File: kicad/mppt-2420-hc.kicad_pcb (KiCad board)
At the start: 4 copper layers, 100 x 100 mm, 141 parts, among them J1 MKDS 5/ 2-9,5, J2 MKDS 5/ 2-9,5, J4 8P8C, J5 8P8C, J7 UEXT, P1 CONN_01X02, Q1 IPA045N10N3G, Q2 IPA045N10N3G, Q3 IPA045N10N3G, T1 BC846B, T10 BC846B, T3 BC846B, T4 BC856B, U1 LM5107, U2 STM32G431CBTx, U3 MPQ8112, U4 LMR16006X, U6 W25Q80DVS, U7 TCAN334, Y1 8MHz

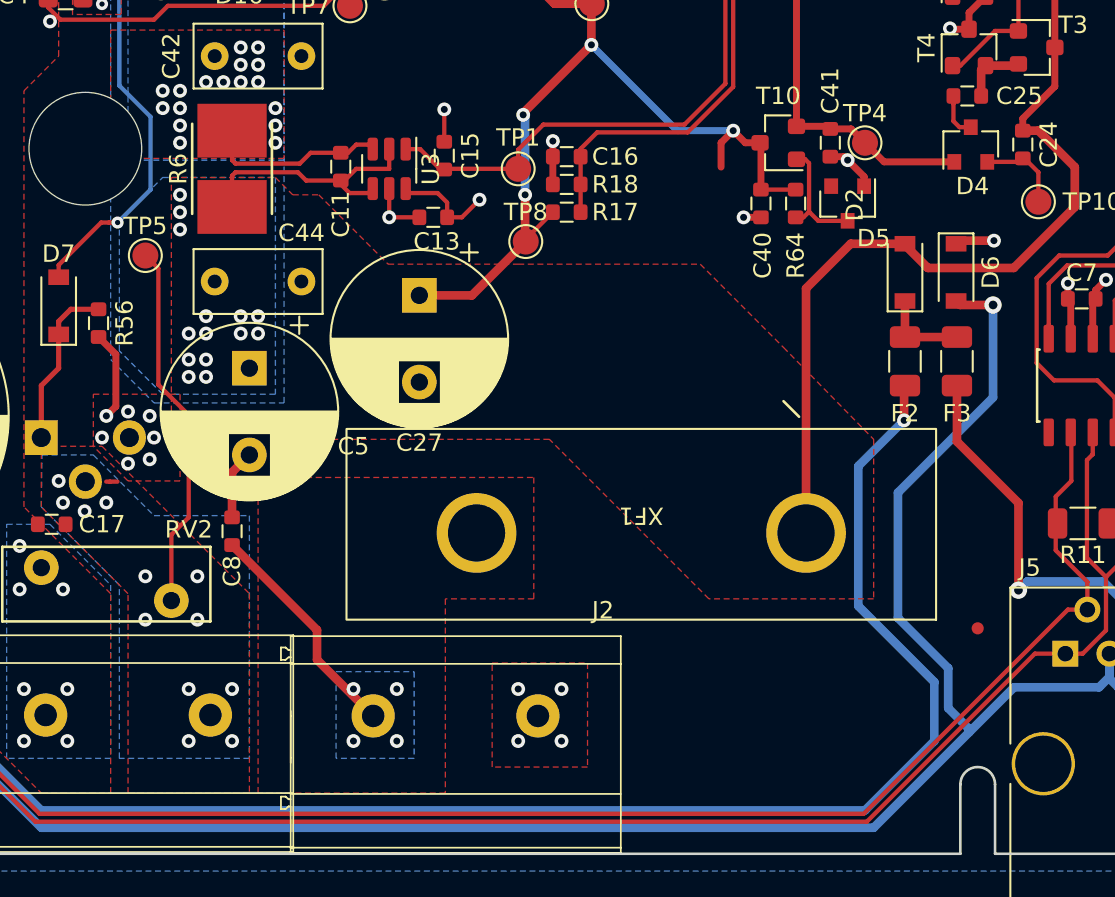
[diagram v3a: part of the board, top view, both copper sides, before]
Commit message: minor component name fix
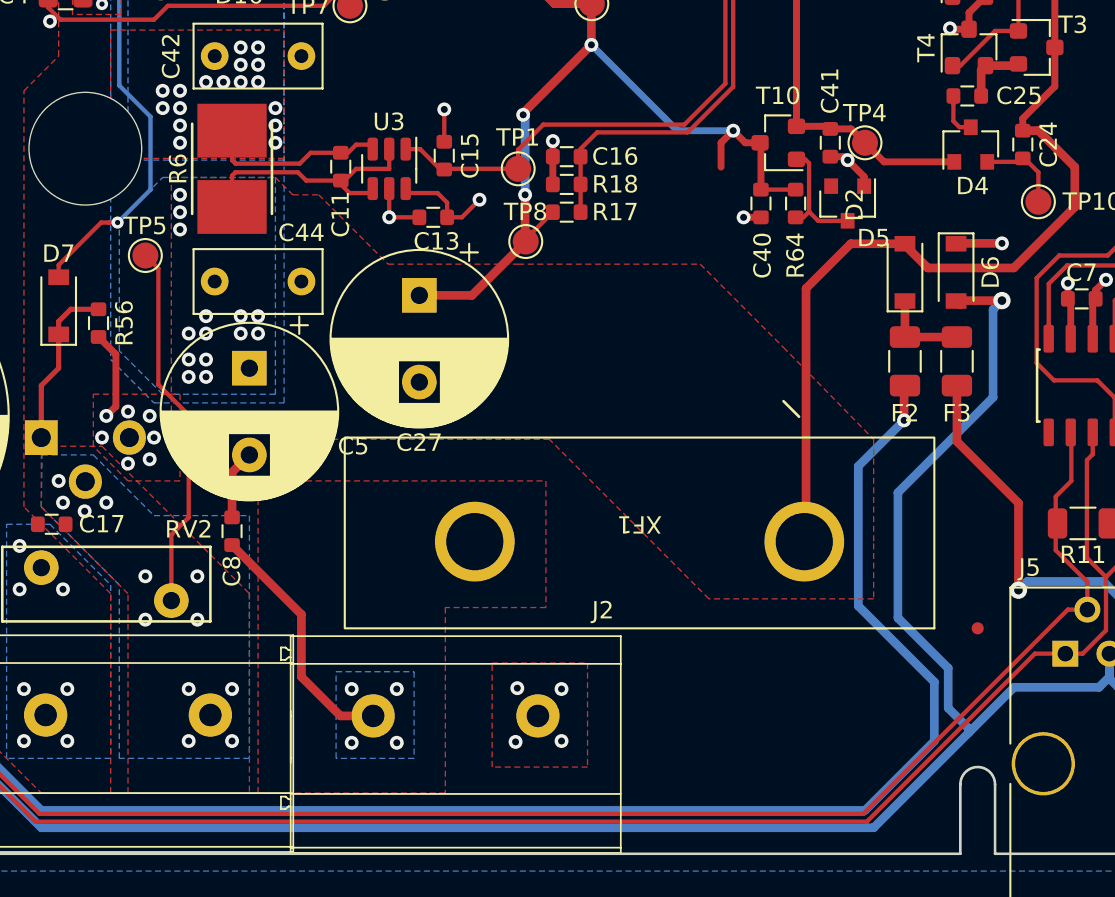
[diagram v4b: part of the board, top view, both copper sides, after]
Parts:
- XF1: footprint LibreSolar:Eaton_S-400 -> LibreSolar:Eaton_S-4000
- moved XF1 0.51 mm to (160.5, 122.0)
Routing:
- net /CAN_GND: track 128.3 -> 129.5 mm
- net /BAT+: track 13.2 -> 14.3 mm
- net /DCDC_HV-: track 22.0 -> 21.3 mm
- net GND: track 73.7 -> 74.4 mm
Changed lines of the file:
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@@
     )
   )
-  (footprint "LibreSolar:Eaton_S-400" (layer "F.Cu")
-    (at 160.6 121.5 180)
+  (footprint "LibreSolar:Eaton_S-4000" (layer "F.Cu")
+    (at 160.5 122 180)
     (property "Manufacturer" "Eaton")
     (property "PartNumber" "")
@@
     (property "Sheetname" "DC/DC")
     (attr smd)
-    (fp_text reference "U3" (at 0 -2.4 90) (layer "F.SilkS")
+    (fp_text reference "U3" (at -2.703 0.013) (layer "F.SilkS")
       (effects (font (size 1 1) (thickness 0.15)))
     )
@@
   (segment (start 185 79.3) (end 185 80.3) (width 0.4) (layer "F.Cu") (net 1))
   (segment (start 178.45 92.45) (end 178.4 92.4) (width 0.4) (layer "F.Cu") (net 1))
-  (segment (start 180.9372 104.6432) (end 178.9316 104.6432) (width 0.5) (layer "F.Cu") (net 1))
   (segment (start 175.1 71.4) (end 175.1 71.85) (width 0.25) (layer "F.Cu") (net 1))
   (segment (start 182.3 60.5) (end 183.300004 60.5) (width 0.25) (layer "F.Cu") (net 1))
@@
   (segment (start 171.5 99.8) (end 172.3 99.8) (width 0.4) (layer "F.Cu") (net 1))
   (segment (start 129.75 114.75) (end 130.3 114.2) (width 0.4) (layer "F.Cu") (net 1))
+  (segment (start 178.7748 104.8) (end 178.7528 104.822) (width 0.5) (layer "F.Cu") (net 1))
   (segment (start 179.5 92.45) (end 178.45 92.45) (width 0.4) (layer "F.Cu") (net 1))
   (segment (start 175.1 72.45) (end 174.85 72.2) (width 0.25) (layer "F.Cu") (net 1))
@@
   (segment (start 190.905 84.895) (end 190.9 84.9) (width 0.4) (layer "F.Cu") (net 1))
   (segment (start 168.2 62.3) (end 166.5 62.3) (width 0.4) (layer "F.Cu") (net 1))
+  (segment (start 181.4 104.8) (end 178.7748 104.8) (width 0.5) (layer "F.Cu") (net 1))
   (segment (start 175.1 71.4) (end 175.1 69.9) (width 0.25) (layer "F.Cu") (net 1))
   (segment (start 186.8 108) (end 186.8 107.499996) (width 0.4) (layer "F.Cu") (net 1))
@@
   (via (at 182 76.8) (size 0.8) (drill 0.4) (layers "F.Cu" "B.Cu") (net 1))
   (via (at 186.3 75.5) (size 0.8) (drill 0.4) (layers "F.Cu" "B.Cu") (net 1))
-  (via (at 180.9372 104.6432) (size 0.8) (drill 0.4) (layers "F.Cu" "B.Cu") (net 1))
+  (via (at 181.4 104.8) (size 0.8) (drill 0.4) (layers "F.Cu" "B.Cu") (net 1))
   (via (at 116.5 117) (size 0.8) (drill 0.4) (layers "F.Cu" "B.Cu") (net 1))
   (via (at 124.8 81.2) (size 0.8) (drill 0.4) (layers "F.Cu" "B.Cu") (net 1))
   (via (at 129.5 91) (size 0.7) (drill 0.3) (layers "F.Cu" "B.Cu") (net 1))
   (via (at 187.8 61.7) (size 0.8) (drill 0.4) (layers "F.Cu" "B.Cu") (net 1))
-  (via (at 153.5 130.5) (size 0.8) (drill 0.4) (layers "F.Cu" "B.Cu") (net 1))
+  (via (at 153.45 130.45) (size 0.8) (drill 0.4) (layers "F.Cu" "B.Cu") (net 1))
   (via (at 132.25 117.25) (size 0.8) (drill 0.4) (layers "F.Cu" "B.Cu") (net 1))
   (via (at 172.5 57.7) (size 0.8) (drill 0.4) (layers "F.Cu" "B.Cu") (net 1))
@@
   (via (at 161.6 87.7) (size 0.8) (drill 0.4) (layers "F.Cu" "B.Cu") (net 1))
   (via (at 149.238 97.074) (size 0.8) (drill 0.4) (layers "F.Cu" "B.Cu") (net 1))
-  (via (at 153.5 133.5) (size 0.8) (drill 0.4) (layers "F.Cu" "B.Cu") (net 1))
+  (via (at 153.35 133.55) (size 0.8) (drill 0.4) (layers "F.Cu" "B.Cu") (net 1))
   (via (at 183.300004 60.5) (size 0.8) (drill 0.4) (layers "F.Cu" "B.Cu") (net 1))
   (via (at 108 97.5) (size 0.8) (drill 0.4) (layers "F.Cu" "B.Cu") (net 1))
@@
   (segment (start 164.850011 87.750011) (end 165.449989 88.349989) (width 0.25) (layer "F.Cu") (net 30))
   (segment (start 170.897887 63.75) (end 168.3 66.347887) (width 0.25) (layer "F.Cu") (net 30))
-  (segment (start 141.9 127.1) (end 141.9 128.811) (width 0.5) (layer "F.Cu") (net 31))
-  (segment (start 141.9 128.811) (end 145.139 132.05) (width 0.5) (layer "F.Cu") (net 31))
-  (segment (start 137 122.2) (end 141.9 127.1) (width 0.5) (layer "F.Cu") (net 31))
-  (via (at 146.5 133.5) (size 0.8) (drill 0.4) (layers "F.Cu" "B.Cu") (net 31))
-  (via (at 144 130.5) (size 0.8) (drill 0.4) (layers "F.Cu" "B.Cu") (net 31))
+  (segment (start 145.139 132.05) (end 143.25 132.05) (width 0.5) (layer "F.Cu") (net 31))
+  (segment (start 141 129.8) (end 141 126.2) (width 0.5) (layer "F.Cu") (net 31))
+  (segment (start 143.25 132.05) (end 141 129.8) (width 0.5) (layer "F.Cu") (net 31))
+  (segment (start 141 126.2) (end 137 122.2) (width 0.5) (layer "F.Cu") (net 31))
+  (via (at 146.5 133.6) (size 0.8) (drill 0.4) (layers "F.Cu" "B.Cu") (net 31))
+  (via (at 143.9 130.5) (size 0.8) (drill 0.4) (layers "F.Cu" "B.Cu") (net 31))
   (via (at 146.5 130.5) (size 0.8) (drill 0.4) (layers "F.Cu" "B.Cu") (net 31))
-  (via (at 144 133.5) (size 0.8) (drill 0.4) (layers "F.Cu" "B.Cu") (net 31))
+  (via (at 143.9 133.6) (size 0.8) (drill 0.4) (layers "F.Cu" "B.Cu") (net 31))
   (segment (start 127 112) (end 127 110.05) (width 0.3) (layer "F.Cu") (net 32))
   (segment (start 126 116) (end 126 113) (width 0.3) (layer "F.Cu") (net 32))
@@
   (segment (start 162.670144 98.3) (end 157.722412 93.352268) (width 0.4) (layer "B.Cu") (net 37))
   (segment (start 152.799994 81.465685) (end 152.799994 80.9) (width 0.5) (layer "B.Cu") (net 37))
-  (segment (start 129.96 118.54) (end 129.7425 118.54) (width 0.25) (layer "F.Cu") (net 38))
-  (segment (start 130.394171 118.54) (end 129.96 118.54) (width 0.25) (layer "F.Cu") (net 38))
   (segment (start 134.5 120.6) (end 133.5 121.6) (width 0.25) (layer "F.Cu") (net 38))
   (segment (start 132.749999 112.949999) (end 134.5 114.7) (width 0.25) (layer "F.Cu") (net 38))
@@
   (via (at 137.5 95.5) (size 0.8) (drill 0.4) (layers "F.Cu" "B.Cu") (net 47))
   (via (at 136.5 74.5) (size 0.8) (drill 0.4) (layers "F.Cu" "B.Cu") (net 47))
-  (segment (start 180.8864 108.3516) (end 178.9824 108.3516) (width 0.5) (layer "F.Cu") (net 48))
+  (segment (start 178.7748 108.1) (end 178.7528 108.122) (width 0.5) (layer "F.Cu") (net 48))
   (segment (start 178.9824 108.3516) (end 178.7528 108.122) (width 0.5) (layer "F.Cu") (net 48))
-  (via (at 180.8864 108.3516) (size 1) (drill 0.5) (layers "F.Cu" "B.Cu") (net 48))
+  (segment (start 181.4 108.1) (end 178.7748 108.1) (width 0.5) (layer "F.Cu") (net 48))
+  (via (at 181.4 108.1) (size 1) (drill 0.5) (layers "F.Cu" "B.Cu") (net 48))
   (segment (start 112.925001 129.209999) (end 113.675 128.46) (width 0.5) (layer "B.Cu") (net 48))
   (segment (start 187 130.4) (end 187.595 129.805) (width 0.5) (layer "B.Cu") (net 48))
   (segment (start 187.595 129.805) (end 187.595 128.46) (width 0.5) (layer "B.Cu") (net 48))
-  (segment (start 178.3 129.3) (end 178.3 131.6) (width 0.5) (layer "B.Cu") (net 48))
-  (segment (start 180.8864 113.6856) (end 175.4 119.172) (width 0.5) (layer "B.Cu") (net 48))
+  (segment (start 179.5 132.8) (end 179.5 133) (width 0.5) (layer "B.Cu") (net 48))
+  (segment (start 180.8864 108.6136) (end 180.8864 113.6856) (width 0.5) (layer "B.Cu") (net 48))
   (segment (start 188.1 130.4) (end 192.1 130.4) (width 0.5) (layer "B.Cu") (net 48))
   (segment (start 108.595 128.46) (end 109.795001 129.660001) (width 0.5) (layer "B.Cu") (net 48))
-  (segment (start 179.5 132.8) (end 179.5 133) (width 0.5) (layer "B.Cu") (net 48))
+  (segment (start 178.3 129.3) (end 178.3 131.6) (width 0.5) (layer "B.Cu") (net 48))
+  (segment (start 175.4 126.4) (end 178.3 129.3) (width 0.5) (layer "B.Cu") (net 48))
   (segment (start 174 138.5) (end 179.5 133) (width 0.5) (layer "B.Cu") (net 48))
+  (segment (start 180.8864 113.6856) (end 175.4 119.172) (width 0.5) (layer "B.Cu") (net 48))
   (segment (start 113.675 128.46) (end 115.965017 128.46) (width 0.5) (layer "B.Cu") (net 48))
   (segment (start 109.795001 129.660001) (end 112.474999 129.660001) (width 0.5) (layer "B.Cu") (net 48))
@@
   (segment (start 178.3 131.6) (end 179.5 132.8) (width 0.5) (layer "B.Cu") (net 48))
   (segment (start 126.005017 138.5) (end 174 138.5) (width 0.5) (layer "B.Cu") (net 48))
-  (segment (start 175.4 119.172) (end 175.4 126.4) (width 0.5) (layer "B.Cu") (net 48))
   (segment (start 192.1 130.4) (end 192.675 129.825) (width 0.5) (layer "B.Cu") (net 48))
-  (segment (start 180.8864 108.3516) (end 180.8864 113.6856) (width 0.5) (layer "B.Cu") (net 48))
+  (segment (start 175.4 119.172) (end 175.4 126.4) (width 0.5) (layer "B.Cu") (net 48))
   (segment (start 192.675 129.825) (end 192.675 128.46) (width 0.5) (layer "B.Cu") (net 48))
   (segment (start 112.474999 129.660001) (end 112.925001 129.209999) (width 0.5) (layer "B.Cu") (net 48))
-  (segment (start 175.4 126.4) (end 178.3 129.3) (width 0.5) (layer "B.Cu") (net 48))
   (segment (start 115.965017 128.46) (end 126.005017 138.5) (width 0.5) (layer "B.Cu") (net 48))
   (segment (start 187.595 128.46) (end 187.595 129.895) (width 0.5) (layer "B.Cu") (net 48))
+  (segment (start 181.4 108.1) (end 180.8864 108.6136) (width 0.5) (layer "B.Cu") (net 48))
   (segment (start 185.4 118.5) (end 184.5 119.4) (width 0.25) (layer "F.Cu") (net 49))
   (segment (start 173.42109 137.7) (end 185.20109 125.92) (width 0.25) (layer "F.Cu") (net 49))
@@
     (polygon
       (pts
-        (xy 154.4 125.3)
-        (xy 149.3 125.3)
+        (xy 155.1 125.8)
+        (xy 149.3 125.8)
         (xy 149.3 136.5)
         (xy 138.5 136.5)
-        (xy 138.5 118.3)
-        (xy 154.4 118.3)
+        (xy 138.5 118.5)
+        (xy 155.1 118.5)
       )
     )
